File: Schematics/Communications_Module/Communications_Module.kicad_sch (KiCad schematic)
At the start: 76 parts, among them J2 SWD_01x04_Pin, J3 Stack Male Edge Connector, J4 USB_C_Female_USB2_Small, Q1 AO3400A, SW1 SW_STM_RESET, SW2 SW_STM_BOOT_MODE, U1 RFM95W-915S2, U12 AMS1117-3.3, U2 W25Q128JVS, U4 LM66100DCKR, U5 LM66100DCKR, U6 LM66100DCKR, U7 STM32F103CBT6, U8 CP2102N-Axx-xQFN28, U9 ISO1042BDWVR, Y1 X322516MMB4SI

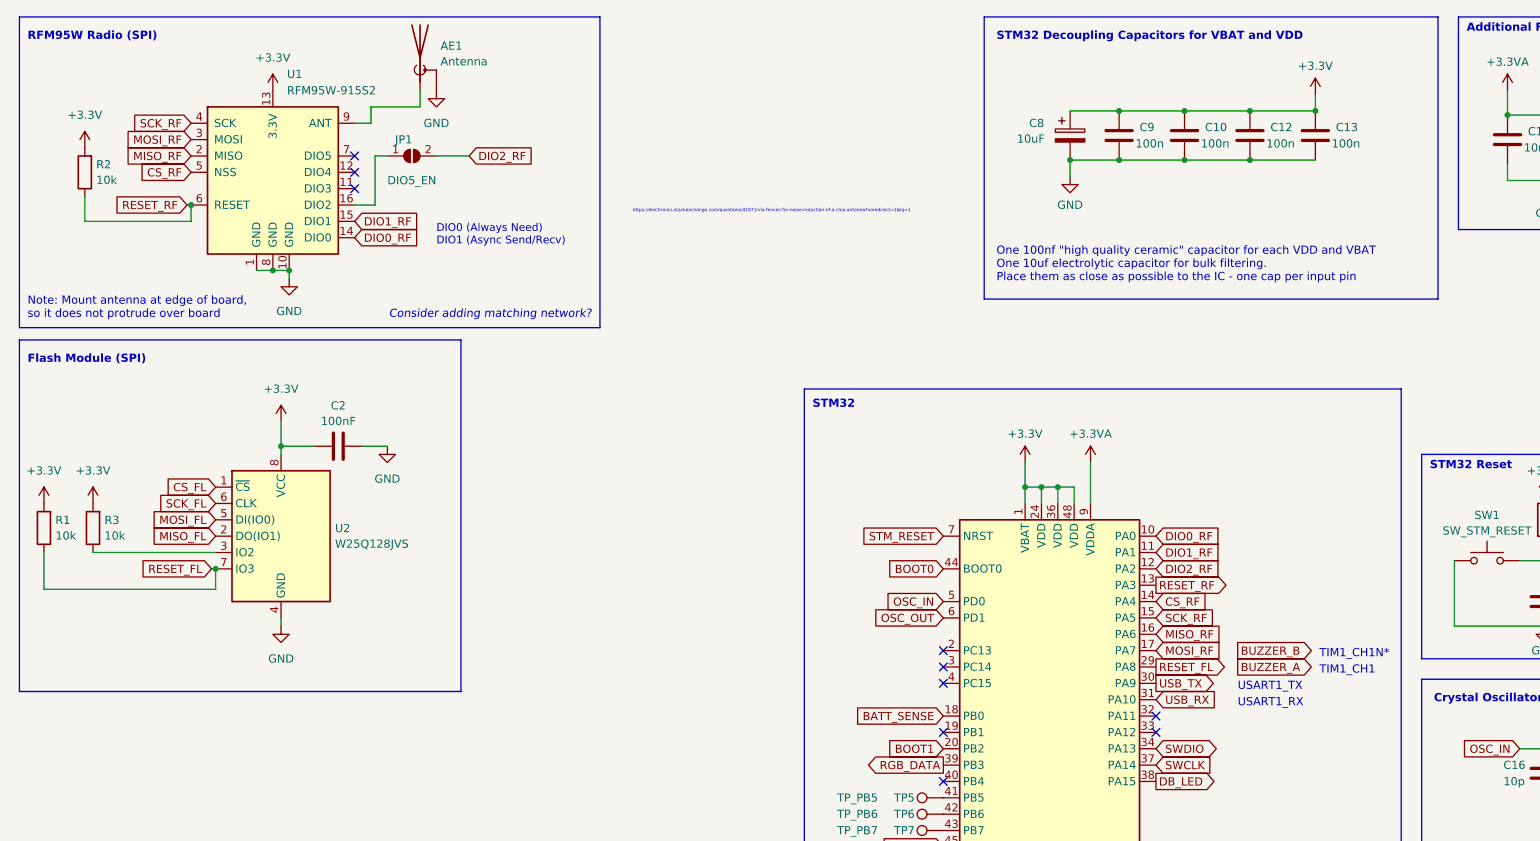
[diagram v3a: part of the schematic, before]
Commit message: Replaced LoRa radio with upgraded module
Replaced RFM65W radio (0.1W) with a LoRa1262F30 radio (1.0W) to schematic
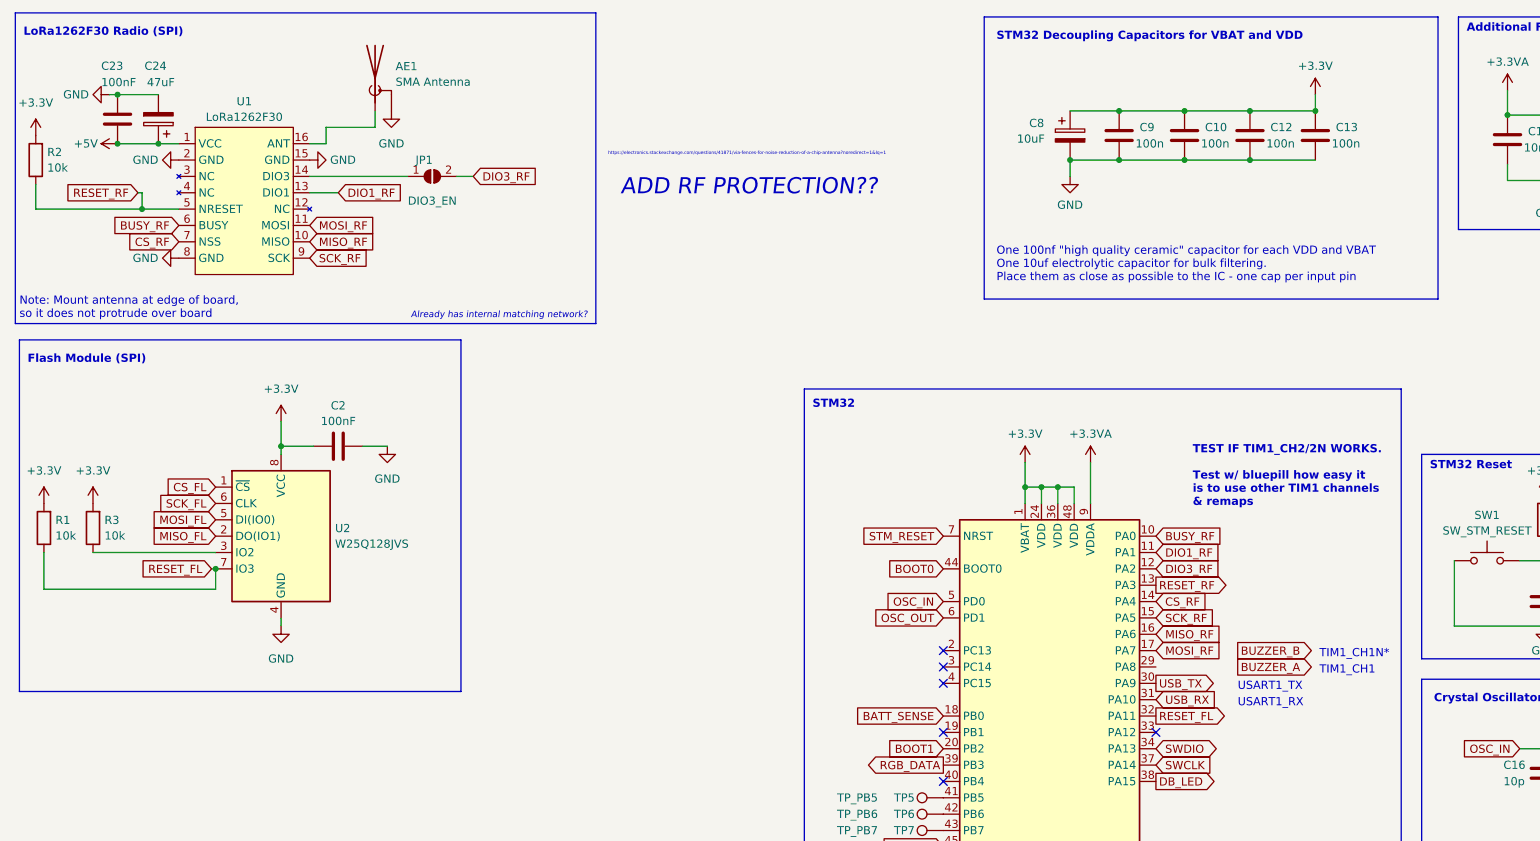
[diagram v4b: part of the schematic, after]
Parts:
- removed U1: RFM95W-915S2, footprints:RFM95W, symbol RF_Module:RFM95W-915S2
- added C23: 100nF, Capacitor_SMD:C_0603_1608Metric, symbol Device:C
- added C24: 47uF, Capacitor_SMD:CP_Elec_4x5.4, symbol Device:C_Polarized
- added U1: LoRa1262F30, footprints:LoRa1262F30, symbol LoRa1262F30:LoRa1262F30
- AE1: value Antenna -> SMA Antenna
- JP1: value DIO5_EN -> DIO3_EN
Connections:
- net +5V: now also C23.2, C24.1, U1.1 (VCC)
- net CS_RF: now also U1.7 (NSS)
- net DIO1_RF: now also U1.13 (DIO1)
- net GND: now also C23.1, C24.2, U1.15 (GND), U1.2 (GND), U1.8 (GND)
- net MISO_RF: now also U1.10 (MISO)
- net MOSI_RF: now also U1.11 (MOSI)
- net RESET_FL: now also U7.32 (PA11); no longer U7.29 (PA8)
- net RESET_RF: now also U1.5 (NRESET)
- net SCK_RF: now also U1.9 (SCK)
- net at JP1.1 (A): now also U1.14 (DIO3)
- net at AE1.1 (A): now also U1.16 (ANT)
- net DIO0_RF renamed BUSY_RF
- net BUSY_RF: now also U1.6 (BUSY)
- net DIO2_RF renamed DIO3_RF
- no-connect marks 38 -> 34
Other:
- note added: "ADD RF PROTECTION??"
- note added: "Already has internal matching network?"
- note added: "LoRa1262F30 Radio (SPI)"
- note added: "TEST IF TIM1_CH2/2N WORKS. Test w/ bluepill how easy it is to use other TIM1 channels & remaps"
- note removed: "Consider adding matching network?"
- note removed: "DIO0 (Always Need) DIO1 (Async Send/Recv)"
- note removed: "RFM95W Radio (SPI)"
- moved on the sheet: AE1, JP1, R2

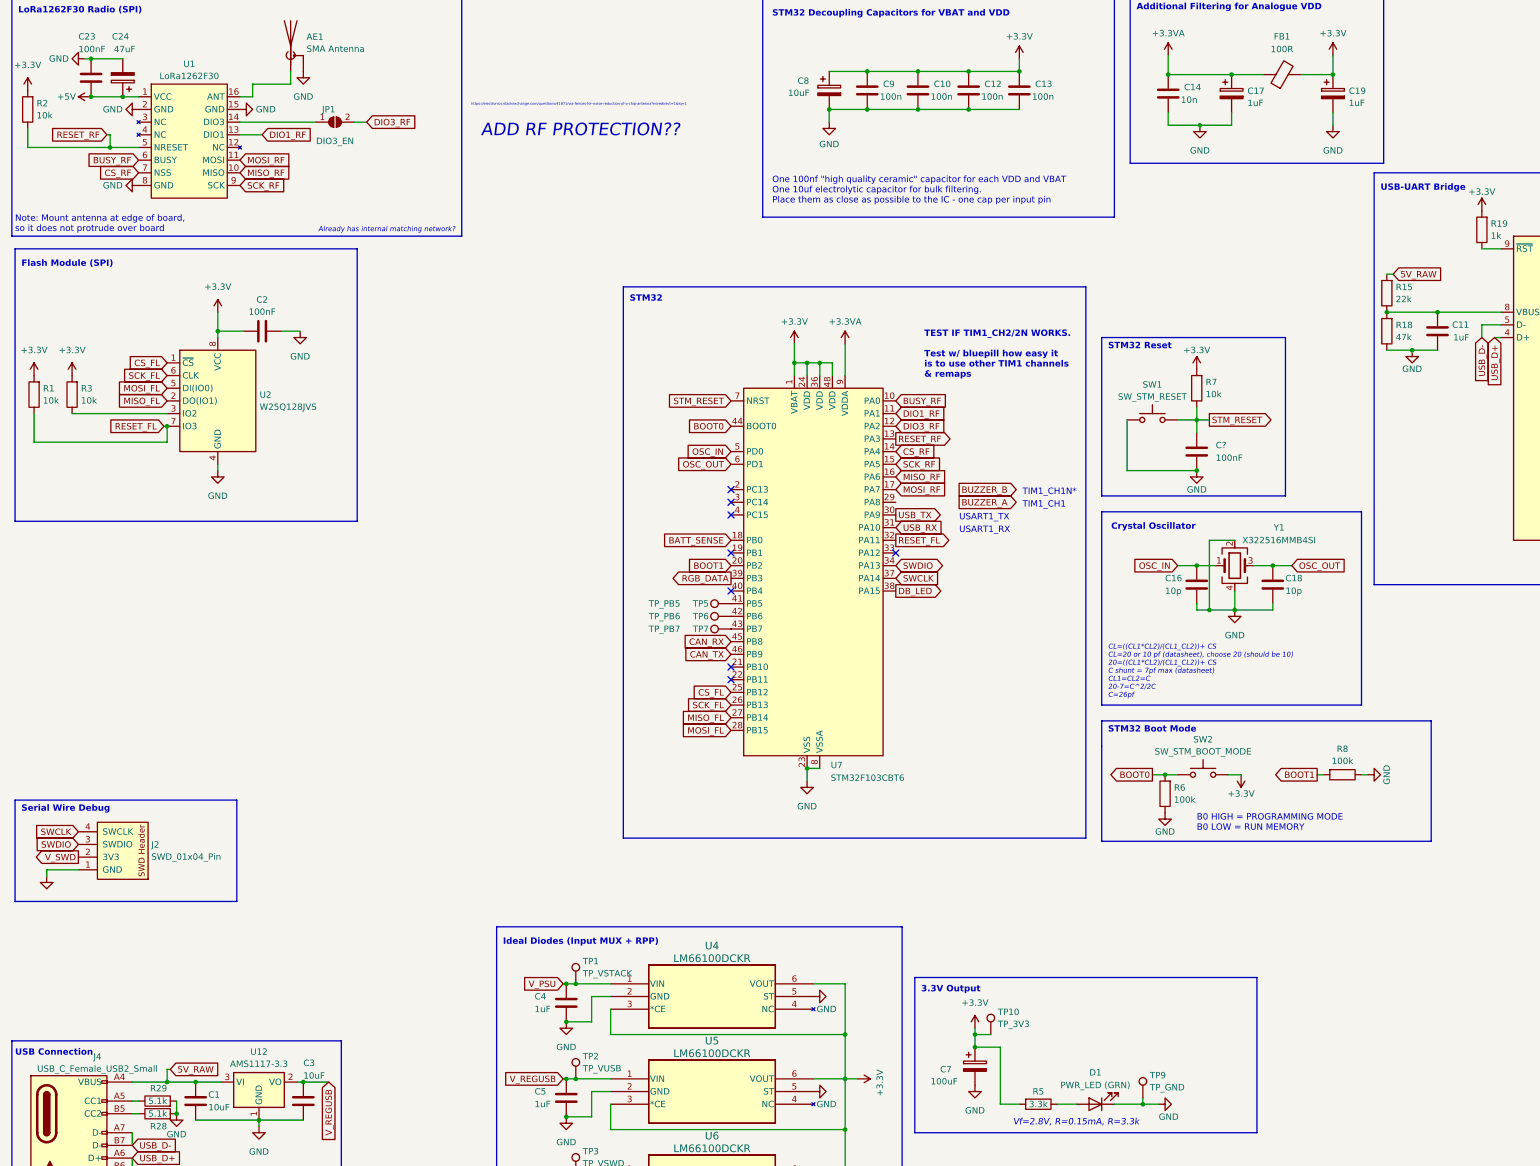
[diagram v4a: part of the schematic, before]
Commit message: Added power MUX for 5V system
This is to allow the LoRa1262F30 to operate while running only on 5V USB power, allowing for much easier debugging.
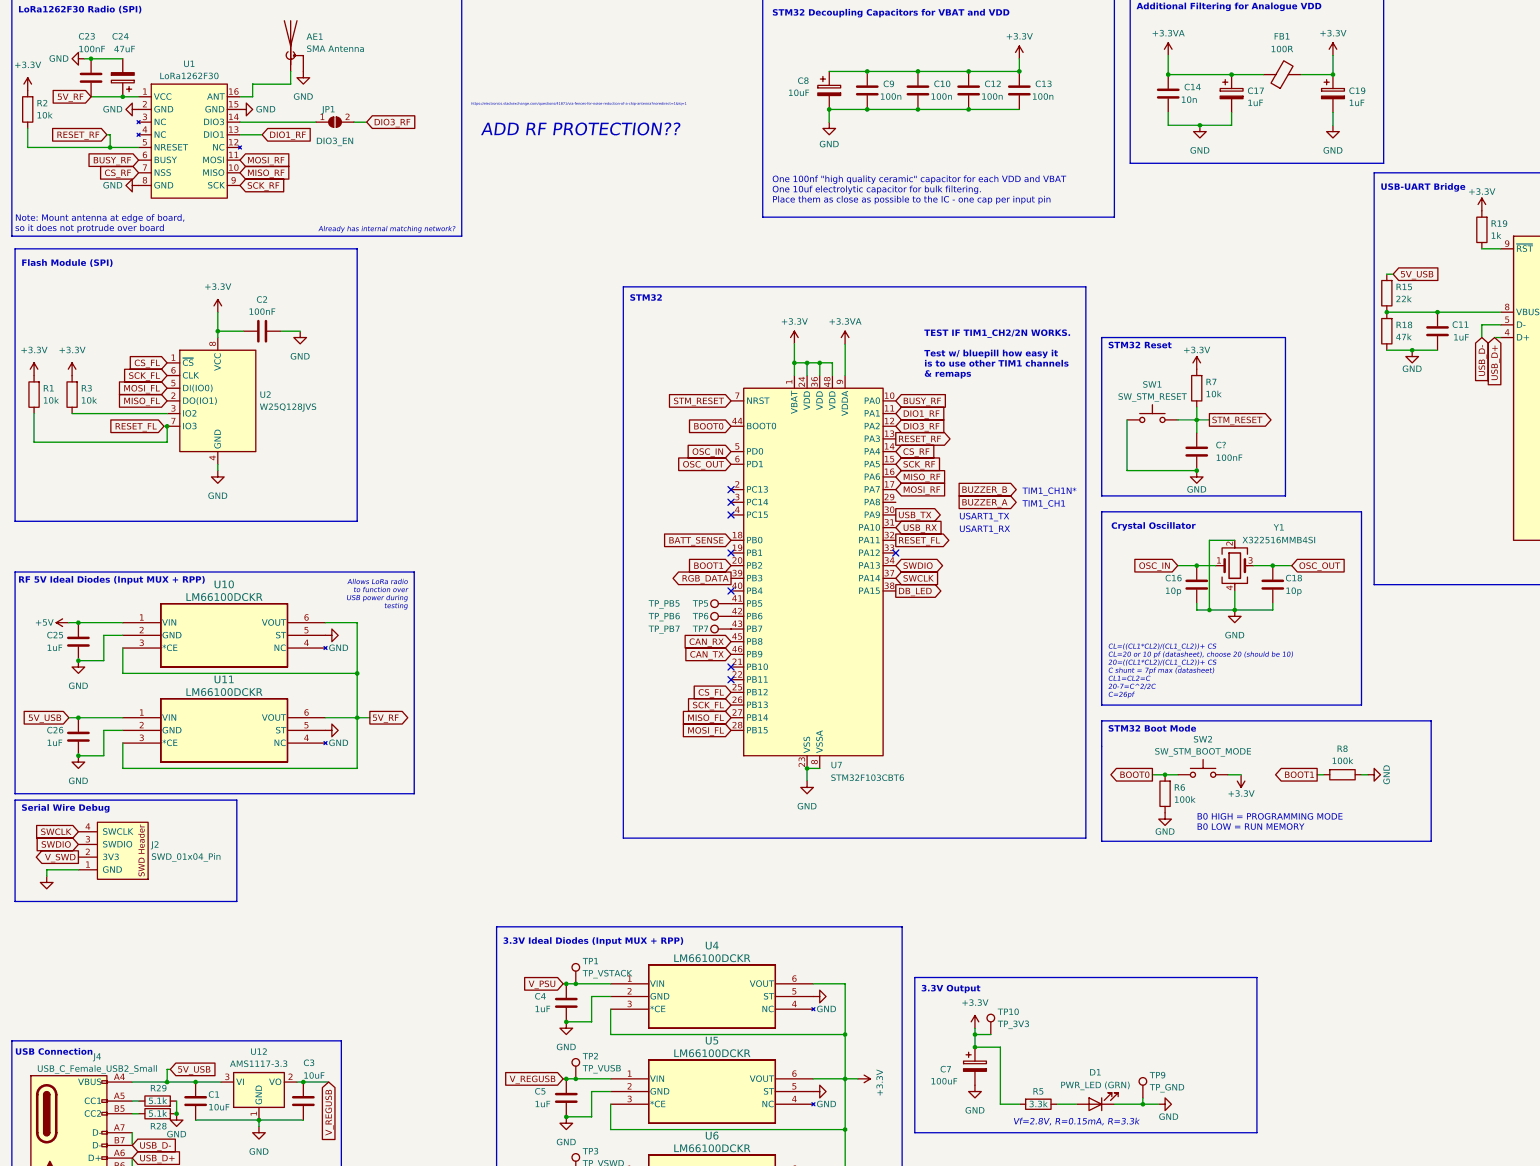
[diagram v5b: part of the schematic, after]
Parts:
- added C25, C26: 1uF, Capacitor_SMD:C_0603_1608Metric, symbol Device:C
- added U10, U11: LM66100DCKR, LMR66100:SC-70-6_Handsoldering, symbol QRET_Buck_PSU:LM66100DCKR
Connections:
- net +5V: now also C25.1, U10.1 (VIN); no longer C23.2, C24.1, U1.1 (VCC)
- net GND: now also C25.2, C26.2, U10.2 (GND), U10.5 (ST), U11.2 (GND), U11.5 (ST)
- net 5V_RAW renamed 5V_USB
- net 5V_USB: now also C26.1, U11.1 (VIN)
- new net 5V_RF: C23.2, C24.1, U1.1 (VCC), U10.3 (*CE), U10.6 (VOUT), U11.3 (*CE), U11.6 (VOUT)
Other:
- note added: "3.3V Ideal Diodes (Input MUX + RPP)"
- note added: "Allows LoRa radio to function over USB power during testing"
- note added: "RF 5V Ideal Diodes (Input MUX + RPP)"
- note removed: "Ideal Diodes (Input MUX + RPP)"

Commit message: Replaced all "LCSC" fields with "JLCPCB" fields
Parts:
- C1, C3: JLCPCB (none) -> C96446; LCSC C96446 -> (none)
- C10, C12, C13, C9: JLCPCB (none) -> C1525; LCSC C1525 -> (none)
- C14: JLCPCB (none) -> C57112; LCSC C57112 -> (none)
- C16, C18: JLCPCB (none) -> C1634; LCSC C1634 -> (none)
- C17, C19: JLCPCB (none) -> C28323; LCSC C28323 -> (none)
- C2, C23, C? (x3): JLCPCB (none) -> C14663; LCSC C14663 -> (none)
- C25, C26, C4, C5, C6: JLCPCB (none) -> C15849; LCSC C15849 -> (none)
- D1: JLCPCB (none) -> C2297; LCSC C2297 -> (none)
- D2, D3: JLCPCB (none) -> C191023; LCSC C191023 -> (none)
- D5: JLCPCB (none) -> C72038; LCSC C72038 -> (none)
- FB1: JLCPCB (none) -> C1015; LCSC C1015 -> (none)
- J4: JLCPCB (none) -> C2936184; LCSC C2936184 -> (none)
- Q1: JLCPCB (none) -> C20917; LCSC C20917 -> (none)
- R1, R10, R14, R2, R3, R7: JLCPCB (none) -> C25804; LCSC C25804 -> (none)
- R11: JLCPCB (none) -> C23228; LCSC C23228 -> (none)
- R12: JLCPCB (none) -> C21190; LCSC C21190 -> (none)
- R13: JLCPCB (none) -> C22984; LCSC C22984 -> (none)
- R28, R29: JLCPCB (none) -> C23186; LCSC C23186 -> (none)
- R4: JLCPCB (none) -> C22843; LCSC C22843 -> (none)
- R5: JLCPCB (none) -> C22978; LCSC C22978 -> (none)
- R6, R8: JLCPCB (none) -> C25803; LCSC C25803 -> (none)
- R9: JLCPCB (none) -> C23193; LCSC C23193 -> (none)
- SW1, SW2: JLCPCB (none) -> C318884; LCSC C318884 -> (none)
- U10, U11, U4, U5, U6: JLCPCB (none) -> C2869734; LCSC C2869734 -> (none)
- U12: JLCPCB (none) -> C6186; LCSC C6186 -> (none)
- U2: JLCPCB (none) -> C97521; LCSC C97521 -> (none)
- U7: JLCPCB (none) -> C8304; LCSC C8304 -> (none)
- U9: JLCPCB (none) -> C484409; LCSC C484409 -> (none)
- Y1: JLCPCB (none) -> C13738; LCSC C13738 -> (none)

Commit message: Added improved buzzer circuit & adjusted pinouts
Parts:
- removed D2, D3: 1N5819WS, Diode_SMD:D_SOD-323, symbol Diode:1N5819WS
- removed Q1: AO3400A, Package_TO_SOT_SMD:SOT-23, symbol Transistor_FET:AO3400A
- removed R10: 10k, Resistor_SMD:R_0603_1608Metric, symbol Device:R
- removed R12: 1k, Resistor_SMD:R_0603_1608Metric, symbol Device:R
- removed R9: 510R, Resistor_SMD:R_0603_1608Metric, symbol Device:R
- added C18: 100nF, Capacitor_SMD:C_0603_1608Metric, symbol Device:C
- added D5, D6: 1N5819WS, Diode_SMD:D_SOD-323, symbol Diode:1N5819WS
- added TP4: PA9, TestPoint:TestPoint_Pad_1.5x1.5mm, symbol Connector:TestPoint
- added U10: TPM8837C-SO1R, footprints:SOP-8_TPK, symbol TPM8837C-SO1R:TPM8837C-SO1R
- BZ1: value PKM13EPYH4000 -> PS1240P02BT; Digikey 490-4698-1-ND -> 445-2525-1-ND
- TP1: value TP_VSTACK -> VSTACK
- TP10: value TP_3V3 -> 3V3
- TP11: value TP_BSENSE -> BSENSE
- TP2: value TP_VUSB -> VUSB
- TP3: value TP_VSWD -> VSWD
- TP5: value TP_PB5 -> PB5
- TP6: value TP_PB6 -> PB6
- TP7: value TP_PB7 -> PB7
- TP9: value TP_GND -> GND
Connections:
- net +3.3V: now also C18.1, D6.2 (A), U10.7 (NSLEEP), U10.8 (VCC)
- net +BATT: now also D5.2 (A)
- net BUZZER_A: now also U7.31 (PA10), U10.6 (IN1)
- net BUZZER_B: now also U7.19 (PB1), U10.5 (IN2)
- net GND: now also C18.2, U10.4 (GND)
- net RESET_FL: now also U7.29 (PA8); no longer U7.32 (PA11)
- net USB_RX: now also U7.21 (PB10); no longer U7.31 (PA10)
- net USB_TX: now also U7.22 (PB11); no longer U7.30 (PA9)
- net at BZ1.1 (-): now also U10.3 (OUT2)
- net at BZ1.2 (+): now also U10.2 (OUT1)
- new net: D5.1 (K), D6.1 (K), U10.1 (VM)
- new net: TP4.1, U7.30 (PA9)
- no-connect marks 34 -> 32
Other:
- note added: "CANRX*"
- note added: "CANTX*"
- note added: "Driving via 2 inverse PWM pins & H-Bridge to effectively double voltage across buzzer"
- note added: "Dual supply input so can test buzzer w/o battery present"
- note added: "PA8 = TIM1_CH1 <all TIM1_CH1N conflict w/ peripheral) PA9 = TIM1_CH2 PB0 = TIM1_CH2N* PA10 = TIM1_CH3 PB1 = TIM1_CH3N*"
- note added: "TIM1_CH3"
- note added: "TIM1_CH3N*"
- note added: "USART3_RX"
- note added: "USART3_TX"
- note removed: "TEST IF TIM1_CH2/2N WORKS. Test w/ bluepill how easy it is to use other TIM1 channels & remaps"
- note removed: "TIM1_CH1"
- note removed: "TIM1_CH1N*"
- note removed: "USART1_RX"
- note removed: "USART1_TX"
- moved on the sheet: C25, C26, C7, D1, J2, R5, TP10, TP9, U10, U11

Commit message: Completed PCB layout
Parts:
- removed JP1: DIO3_EN, Jumper:SolderJumper-2_P1.3mm_Open_RoundedPad1.0x1.5mm, symbol Jumper:SolderJumper_2_Open
- removed TP2: VUSB, TestPoint:TestPoint_Pad_1.5x1.5mm, symbol Connector:TestPoint
- removed TP3: VSWD, TestPoint:TestPoint_Pad_1.5x1.5mm, symbol Connector:TestPoint
- removed TP5: PB5, TestPoint:TestPoint_Pad_1.5x1.5mm, symbol Connector:TestPoint
- TP1: value VSTACK -> VSTAK
- TP11: value BSENSE -> BSENS
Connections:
- net DIO3_RF: now also U1.14 (DIO3)
- net GND: no longer AE1.2 (Shield), U1.15 (GND)
- net Antenna: now reaches AE1.1 (A), U1.16 (ANT)
- new net RF GND: AE1.2 (Shield), U1.15 (GND)
- no-connect marks 32 -> 33
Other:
- note added: "The WS2812B wants min 3.5V, but we're only giving 3.3V. In the past this works fine."
- note removed: "The WS2812B needs at least 3.5V input, but we're only using 3.3V This may cause problems"
